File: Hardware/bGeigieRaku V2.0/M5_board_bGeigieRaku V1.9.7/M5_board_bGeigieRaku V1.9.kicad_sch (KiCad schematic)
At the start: 26 parts, among them J1 M5 2x15 pin, J10 QI GND, J11 QI charger Plus, J2 Geiger, J3 GPS, J4 Geiger 2, J7 Conn_01x14_Female, J8 QI charger GND, J9 QI Plus, Q1 IRF4905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

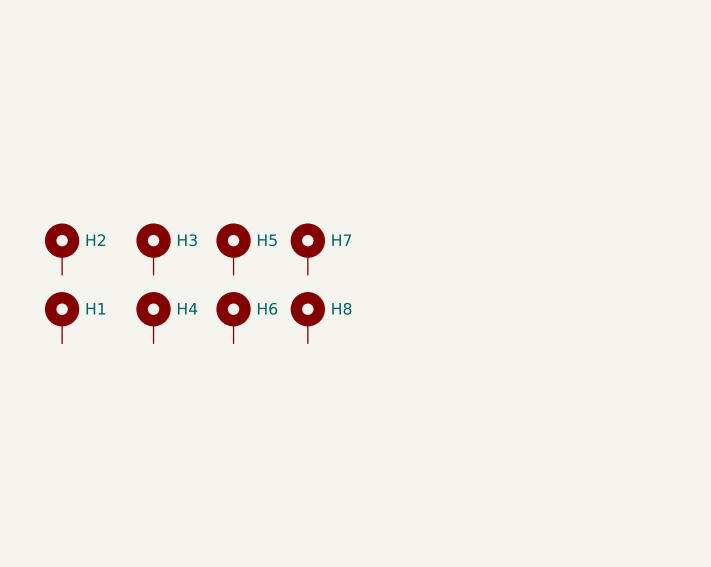
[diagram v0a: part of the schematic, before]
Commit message: alighed holes
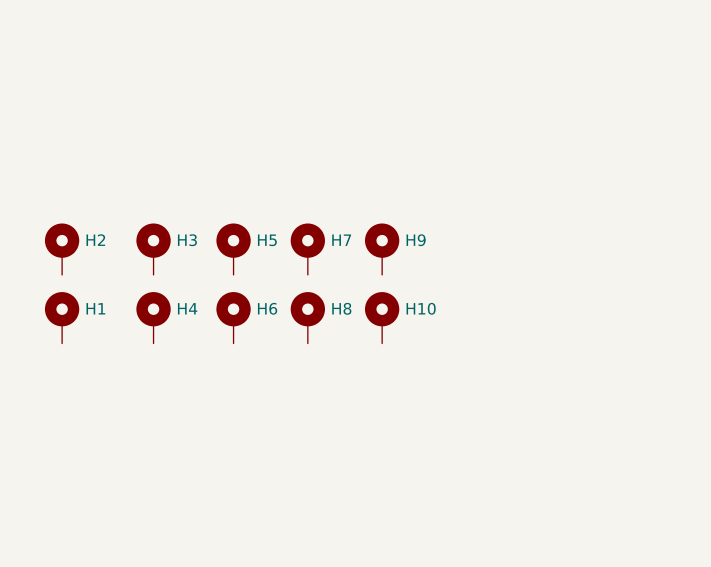
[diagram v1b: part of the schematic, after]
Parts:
- added H10, H9: MountingHole_Pad, MountingHole:MountingHole_3.2mm_M3, symbol Mechanical:MountingHole_Pad
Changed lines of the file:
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@@
+    (pin "1")
+  )
+  (symbol (lib_id "Mechanical:MountingHole_Pad") (at 241.3 116.84 0) (unit 1)
+    (in_bom yes) (on_board yes)
+    (property "Reference" "H9" (id 0) (at 243.84 115.57 0)
+      (effects (font (size 1.27 1.27)) (justify left))
+    )
+    (property "Value" "MountingHole_Pad" (id 1) (at 243.8402 117.8624 0)
+      (effects (font (size 1.27 1.27)) (justify left) hide)
+    )
+    (property "Footprint" "MountingHole:MountingHole_3.2mm_M3" (id 2) (at 241.3 116.84 0)
+      (effects (font (size 1.27 1.27)) hide)
+    )
+    (property "Datasheet" "~" (id 3) (at 241.3 116.84 0)
+      (effects (font (size 1.27 1.27)) hide)
+    )
+    (pin "1")
+  )
+  (symbol (lib_id "Mechanical:MountingHole_Pad") (at 241.3 124.46 0) (unit 1)
+    (in_bom yes) (on_board yes)
+    (property "Reference" "H10" (id 0) (at 243.84 123.19 0)
+      (effects (font (size 1.27 1.27)) (justify left))
+    )
+    (property "Value" "MountingHole_Pad" (id 1) (at 243.8398 125.4822 0)
+      (effects (font (size 1.27 1.27)) (justify left) hide)
+    )
+    (property "Footprint" "MountingHole:MountingHole_3.2mm_M3" (id 2) (at 241.3 124.46 0)
+      (effects (font (size 1.27 1.27)) hide)
+    )
+    (property "Datasheet" "~" (id 3) (at 241.3 124.46 0)
+      (effects (font (size 1.27 1.27)) hide)
+    )
     (pin "1")
   )
@@
       (reference "H8") (unit 1) (value "MountingHole_Pad") (footprint "MountingHole:MountingHole_3.2mm_M3")
     )
+    (path "/cd5e07e4-0c52-4526-99de-27f6a1504ee0"
+      (reference "H9") (unit 1) (value "MountingHole_Pad") (footprint "MountingHole:MountingHole_3.2mm_M3")
+    )
+    (path "/33accb9f-62b7-4730-ac41-d79864f006ad"
+      (reference "H10") (unit 1) (value "MountingHole_Pad") (footprint "MountingHole:MountingHole_3.2mm_M3")
+    )
     (path "/00000000-0000-0000-0000-00005d532c3e"

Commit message: Update V1.9.7 board.
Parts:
- removed D1, D2: DIODE, Diode_THT:D_DO-15_P15.24mm_Horizontal, symbol pspice:DIODE
- removed Q1, Q2: IRF4905, Package_TO_SOT_THT:TO-220-3_Vertical, symbol Transistor_FET:IRF4905
- added D1, D2: 1N4001, Diode_THT:D_DO-41_SOD81_P10.16mm_Horizontal, symbol Diode:1N4001
- added J5: Extra support header, Connector_PinHeader_2.54mm:PinHeader_1x02_P2.54mm_Vertical, symbol Connector:Conn_01x02_Male
- added Q1, Q2: IRFR9024, Package_TO_SOT_THT:TO-251-3_Vertical, symbol IRFR9024:IRFR9024
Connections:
- net GND: now also Q1.1, Q2.1
- net VBATT: now also D2.1 (K), Q2.3
- net at BT1.1 (+): now also D1.1 (K), D2.2 (A), Q1.3, Q2.2
- net at J11.1 (Pin_1), J11.2 (Pin_2): now also D1.2 (A), Q1.2
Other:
- note added: "Fix pin numbers and names on Q1 and Q2"

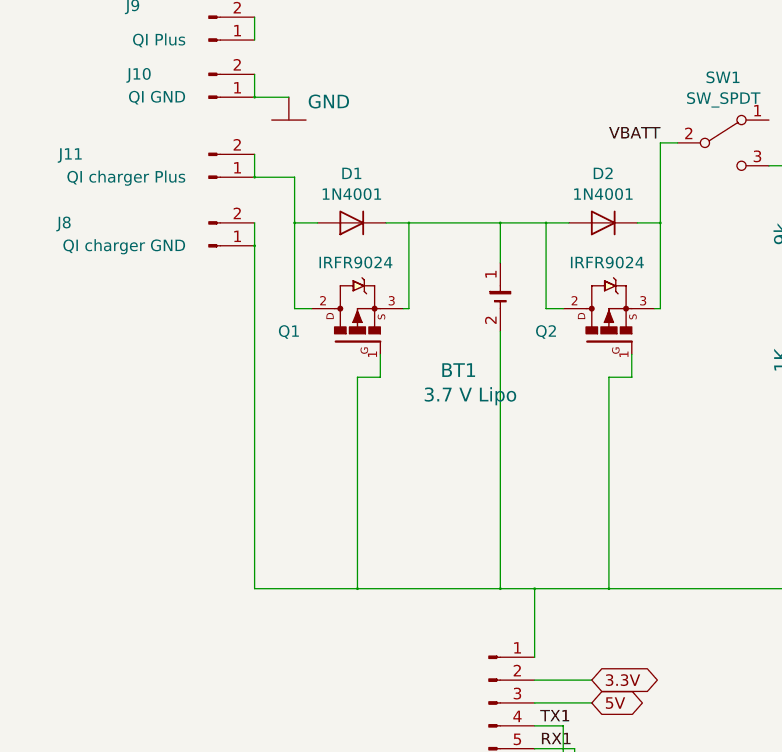
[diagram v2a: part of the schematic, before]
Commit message: Remove  Q1 and D1 (mosfet proteting TP4056)
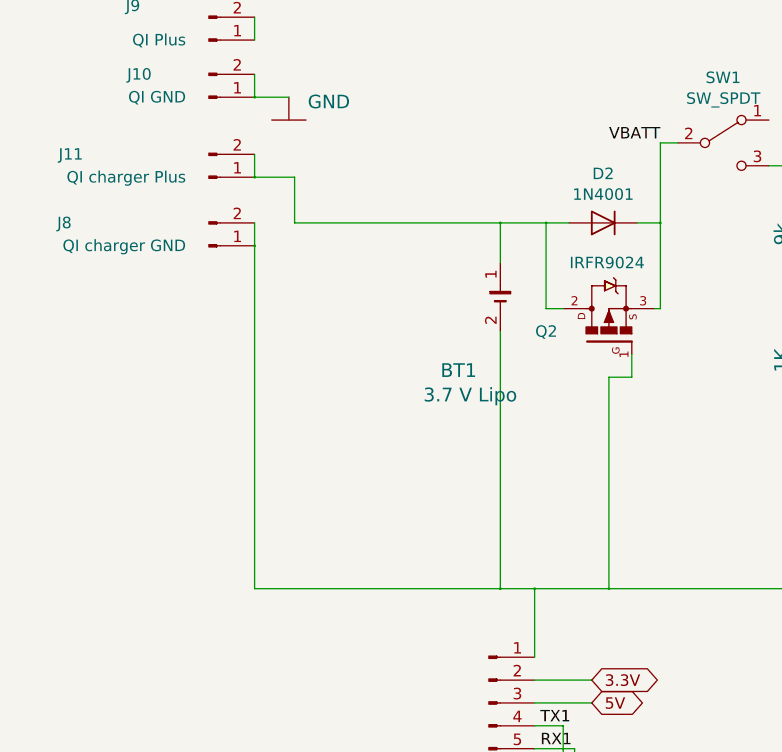
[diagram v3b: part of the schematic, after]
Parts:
- removed D1: 1N4001, Diode_THT:D_DO-41_SOD81_P10.16mm_Horizontal, symbol Diode:1N4001
- removed Q1: IRFR9024, Package_TO_SOT_THT:TO-251-3_Vertical, symbol IRFR9024:IRFR9024
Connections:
- net at BT1.1 (+), D2.2 (A), Q2.2: now also J11.1 (Pin_1), J11.2 (Pin_2)

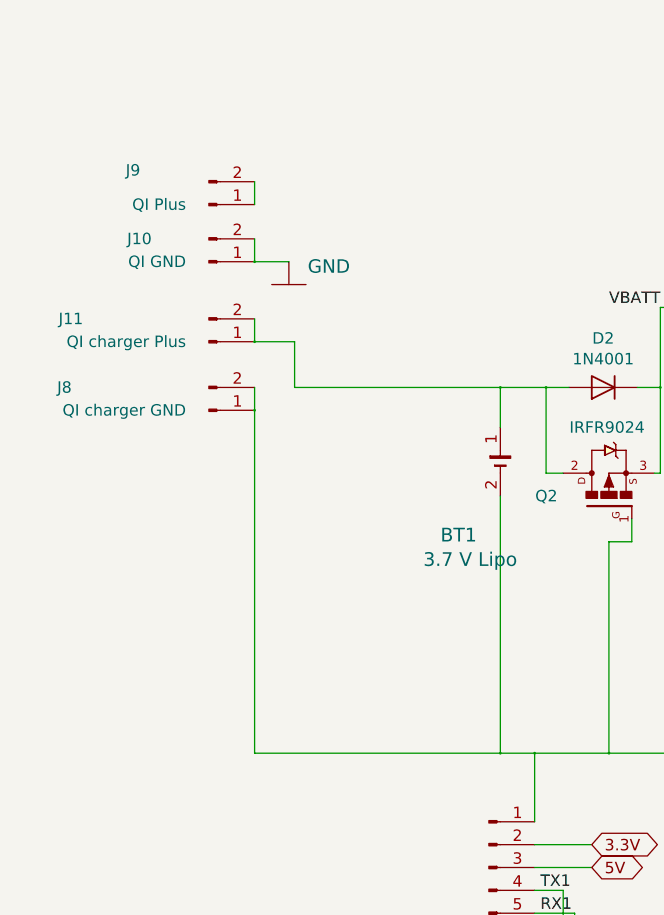
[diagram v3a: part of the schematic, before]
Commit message: Moved display 1mm to the left to get it centered.
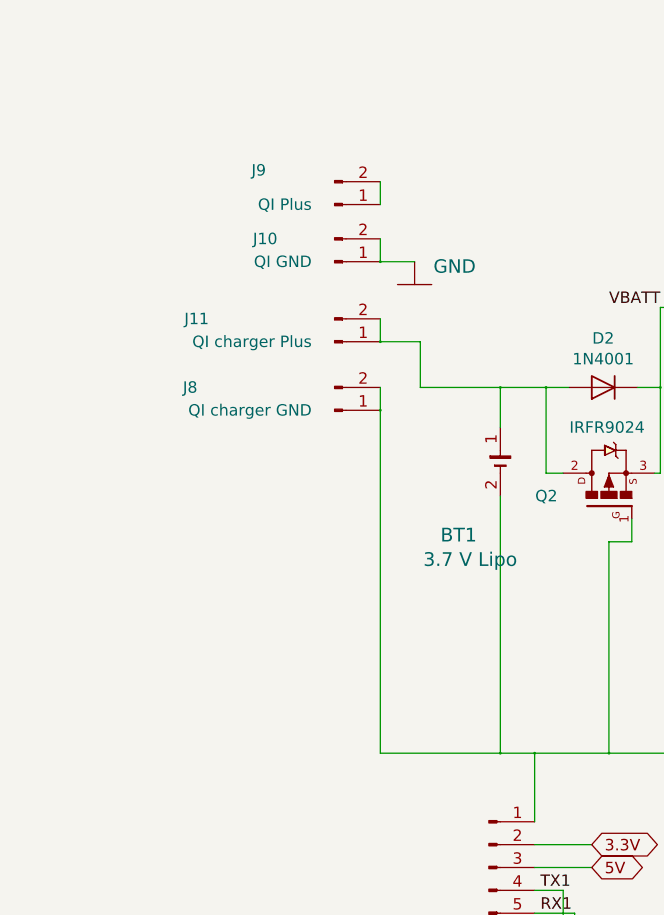
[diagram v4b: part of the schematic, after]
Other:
- moved on the sheet: J10, J11, J8, J9
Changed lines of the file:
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@@
     (date "sam. 04 avril 2015")
   )
-  (junction (at 55.88 71.12) (diameter 0.3048) (color 0 0 0 0))
-  (junction (at 55.88 80.01) (diameter 0.3048) (color 0 0 0 0))
-  (junction (at 55.88 87.63) (diameter 0.3048) (color 0 0 0 0))
+  (junction (at 69.85 71.12) (diameter 0.3048) (color 0 0 0 0))
+  (junction (at 69.85 80.01) (diameter 0.3048) (color 0 0 0 0))
+  (junction (at 69.85 87.63) (diameter 0.3048) (color 0 0 0 0))
   (junction (at 83.185 85.09) (diameter 0.3048) (color 0 0 0 0))
   (junction (at 83.185 125.73) (diameter 0.3048) (color 0 0 0 0))
@@
   (junction (at 186.69 82.55) (diameter 0.3048) (color 0 0 0 0))
   (junction (at 187.96 69.85) (diameter 0.3048) (color 0 0 0 0))
-  (wire (pts (xy 55.88 62.23) (xy 55.88 64.77))
-    (stroke (width 0) (type solid) (color 0 0 0 0))
-  )
-  (wire (pts (xy 55.88 68.58) (xy 55.88 71.12))
-    (stroke (width 0) (type solid) (color 0 0 0 0))
-  )
-  (wire (pts (xy 55.88 71.12) (xy 59.69 71.12))
-    (stroke (width 0) (type solid) (color 0 0 0 0))
-  )
-  (wire (pts (xy 55.88 77.47) (xy 55.88 80.01))
-    (stroke (width 0) (type solid) (color 0 0 0 0))
-  )
-  (wire (pts (xy 55.88 80.01) (xy 60.325 80.01))
-    (stroke (width 0) (type solid) (color 0 0 0 0))
-  )
-  (wire (pts (xy 55.88 85.09) (xy 55.88 87.63))
-    (stroke (width 0) (type solid) (color 0 0 0 0))
-  )
-  (wire (pts (xy 55.88 87.63) (xy 55.88 125.73))
-    (stroke (width 0) (type solid) (color 0 0 0 0))
-  )
-  (wire (pts (xy 55.88 125.73) (xy 83.185 125.73))
-    (stroke (width 0) (type solid) (color 0 0 0 0))
-  )
-  (wire (pts (xy 60.325 80.01) (xy 60.325 85.09))
-    (stroke (width 0) (type solid) (color 0 0 0 0))
-  )
-  (wire (pts (xy 60.325 85.09) (xy 83.185 85.09))
+  (wire (pts (xy 69.85 62.23) (xy 69.85 64.77))
+    (stroke (width 0) (type solid) (color 0 0 0 0))
+  )
+  (wire (pts (xy 69.85 68.58) (xy 69.85 71.12))
+    (stroke (width 0) (type solid) (color 0 0 0 0))
+  )
+  (wire (pts (xy 69.85 71.12) (xy 73.66 71.12))
+    (stroke (width 0) (type solid) (color 0 0 0 0))
+  )
+  (wire (pts (xy 69.85 77.47) (xy 69.85 80.01))
+    (stroke (width 0) (type solid) (color 0 0 0 0))
+  )
+  (wire (pts (xy 69.85 80.01) (xy 74.295 80.01))
+    (stroke (width 0) (type solid) (color 0 0 0 0))
+  )
+  (wire (pts (xy 69.85 85.09) (xy 69.85 87.63))
+    (stroke (width 0) (type solid) (color 0 0 0 0))
+  )
+  (wire (pts (xy 69.85 87.63) (xy 69.85 125.73))
+    (stroke (width 0) (type solid) (color 0 0 0 0))
+  )
+  (wire (pts (xy 69.85 125.73) (xy 83.185 125.73))
+    (stroke (width 0) (type solid) (color 0 0 0 0))
+  )
+  (wire (pts (xy 74.295 80.01) (xy 74.295 85.09))
+    (stroke (width 0) (type solid) (color 0 0 0 0))
+  )
+  (wire (pts (xy 74.295 85.09) (xy 83.185 85.09))
     (stroke (width 0) (type solid) (color 0 0 0 0))
   )
@@
     )
   )
-  (symbol (lib_id "bGeigieRaku-V2-rescue:GND-bGeigieNano_V1.1.5") (at 59.69 73.66 0) (unit 1)
+  (symbol (lib_id "bGeigieRaku-V2-rescue:GND-bGeigieNano_V1.1.5") (at 73.66 73.66 0) (unit 1)
     (in_bom yes) (on_board yes)
-    (property "Reference" "#GND0101" (id 0) (at 59.69 73.66 0)
-      (effects (font (size 1.27 1.27)) hide)
-    )
-    (property "Value" "GND" (id 1) (at 64.135 71.6534 0)
+    (property "Reference" "#GND0101" (id 0) (at 73.66 73.66 0)
+      (effects (font (size 1.27 1.27)) hide)
+    )
+    (property "Value" "GND" (id 1) (at 78.105 71.6534 0)
       (effects (font (size 1.4986 1.4986)))
     )
-    (property "Footprint" "" (id 2) (at 59.69 73.66 0)
-      (effects (font (size 1.27 1.27)) hide)
-    )
-    (property "Datasheet" "" (id 3) (at 59.69 73.66 0)
+    (property "Footprint" "" (id 2) (at 73.66 73.66 0)
+      (effects (font (size 1.27 1.27)) hide)
+    )
+    (property "Datasheet" "" (id 3) (at 73.66 73.66 0)
       (effects (font (size 1.27 1.27)) hide)
     )
@@
     (pin "1")
   )
-  (symbol (lib_id "Connector:Conn_01x02_Male") (at 50.8 64.77 0) (mirror x) (unit 1)
+  (symbol (lib_id "Connector:Conn_01x02_Male") (at 64.77 64.77 0) (mirror x) (unit 1)
     (in_bom yes) (on_board yes)
-    (property "Reference" "J9" (id 0) (at 43.18 60.96 0)
-      (effects (font (size 1.27 1.27)) (justify right))
-    )
-    (property "Value" "QI Plus" (id 1) (at 48.26 64.77 0)
-      (effects (font (size 1.27 1.27)) (justify right))
-    )
-    (property "Footprint" "Connector_PinHeader_2.54mm:PinHeader_1x02_P2.54mm_Vertical" (id 2) (at 50.8 64.77 0)
-      (effects (font (size 1.27 1.27)) hide)
-    )
-    (property "Datasheet" "~" (id 3) (at 50.8 64.77 0)
+    (property "Reference" "J9" (id 0) (at 57.15 60.96 0)
+      (effects (font (size 1.27 1.27)) (justify right))
+    )
+    (property "Value" "QI Plus" (id 1) (at 62.23 64.77 0)
+      (effects (font (size 1.27 1.27)) (justify right))
+    )
+    (property "Footprint" "Connector_PinHeader_2.54mm:PinHeader_1x02_P2.54mm_Vertical" (id 2) (at 64.77 64.77 0)
+      (effects (font (size 1.27 1.27)) hide)
+    )
+    (property "Datasheet" "~" (id 3) (at 64.77 64.77 0)
       (effects (font (size 1.27 1.27)) hide)
     )
@@
     (pin "2")
   )
-  (symbol (lib_id "Connector:Conn_01x02_Male") (at 50.8 71.12 0) (mirror x) (unit 1)
+  (symbol (lib_id "Connector:Conn_01x02_Male") (at 64.77 71.12 0) (mirror x) (unit 1)
     (in_bom yes) (on_board yes)
-    (property "Reference" "J10" (id 0) (at 44.45 68.58 0)
-      (effects (font (size 1.27 1.27)) (justify right))
-    )
-    (property "Value" "QI GND" (id 1) (at 48.26 71.12 0)
-      (effects (font (size 1.27 1.27)) (justify right))
-    )
-    (property "Footprint" "Connector_PinHeader_2.54mm:PinHeader_1x02_P2.54mm_Vertical" (id 2) (at 50.8 71.12 0)
-      (effects (font (size 1.27 1.27)) hide)
-    )
-    (property "Datasheet" "~" (id 3) (at 50.8 71.12 0)
+    (property "Reference" "J10" (id 0) (at 58.42 68.58 0)
+      (effects (font (size 1.27 1.27)) (justify right))
+    )
+    (property "Value" "QI GND" (id 1) (at 62.23 71.12 0)
+      (effects (font (size 1.27 1.27)) (justify right))
+    )
+    (property "Footprint" "Connector_PinHeader_2.54mm:PinHeader_1x02_P2.54mm_Vertical" (id 2) (at 64.77 71.12 0)
+      (effects (font (size 1.27 1.27)) hide)
+    )
+    (property "Datasheet" "~" (id 3) (at 64.77 71.12 0)
       (effects (font (size 1.27 1.27)) hide)
     )
@@
     (pin "2")
   )
-  (symbol (lib_id "Connector:Conn_01x02_Male") (at 50.8 80.01 0) (mirror x) (unit 1)
+  (symbol (lib_id "Connector:Conn_01x02_Male") (at 64.77 80.01 0) (mirror x) (unit 1)
     (in_bom yes) (on_board yes)
-    (property "Reference" "J11" (id 0) (at 36.83 77.47 0)
-      (effects (font (size 1.27 1.27)) (justify right))
-    )
-    (property "Value" "QI charger Plus" (id 1) (at 48.26 80.01 0)
-      (effects (font (size 1.27 1.27)) (justify right))
-    )
-    (property "Footprint" "Connector_PinHeader_2.54mm:PinHeader_1x02_P2.54mm_Vertical" (id 2) (at 50.8 80.01 0)
-      (effects (font (size 1.27 1.27)) hide)
-    )
-    (property "Datasheet" "~" (id 3) (at 50.8 80.01 0)
+    (property "Reference" "J11" (id 0) (at 50.8 77.47 0)
+      (effects (font (size 1.27 1.27)) (justify right))
+    )
+    (property "Value" "QI charger Plus" (id 1) (at 62.23 80.01 0)
+      (effects (font (size 1.27 1.27)) (justify right))
+    )
+    (property "Footprint" "Connector_PinHeader_2.54mm:PinHeader_1x02_P2.54mm_Vertical" (id 2) (at 64.77 80.01 0)
+      (effects (font (size 1.27 1.27)) hide)
+    )
+    (property "Datasheet" "~" (id 3) (at 64.77 80.01 0)
       (effects (font (size 1.27 1.27)) hide)
     )
@@
     (pin "2")
   )
-  (symbol (lib_id "Connector:Conn_01x02_Male") (at 50.8 87.63 0) (mirror x) (unit 1)
+  (symbol (lib_id "Connector:Conn_01x02_Male") (at 64.77 87.63 0) (mirror x) (unit 1)
     (in_bom yes) (on_board yes)
-    (property "Reference" "J8" (id 0) (at 35.56 85.09 0)
-      (effects (font (size 1.27 1.27)) (justify right))
-    )
-    (property "Value" "QI charger GND" (id 1) (at 48.26 87.63 0)
-      (effects (font (size 1.27 1.27)) (justify right))
-    )
-    (property "Footprint" "Connector_PinHeader_2.54mm:PinHeader_1x02_P2.54mm_Vertical" (id 2) (at 50.8 87.63 0)
-      (effects (font (size 1.27 1.27)) hide)
-    )
-    (property "Datasheet" "~" (id 3) (at 50.8 87.63 0)
-      (effects (font (size 1.27 1.27)) hide)
-    )
+    (property "Reference" "J8" (id 0) (at 49.53 85.09 0)
+      (effects (font (size 1.27 1.27)) (justify right))
+    )
+    (property "Value" "QI charger GND" (id 1) (at 62.23 87.63 0)
+      (effects (font (size 1.27 1.27)) (justify right))
+    )
+    (property "Footprint" "Connector_PinHeader_2.54mm:PinHeader_1x02_P2.54mm_Vertical" (id 2) (at 64.77 87.63 0)
+      (effects (font (size 1.27 1.27)) hide)
+    )
+    (property "Datasheet" "~" (id 3) (at 64.77 87.63 0)
+      (effects (font (size 1.27 1.27)) hide)
+    )

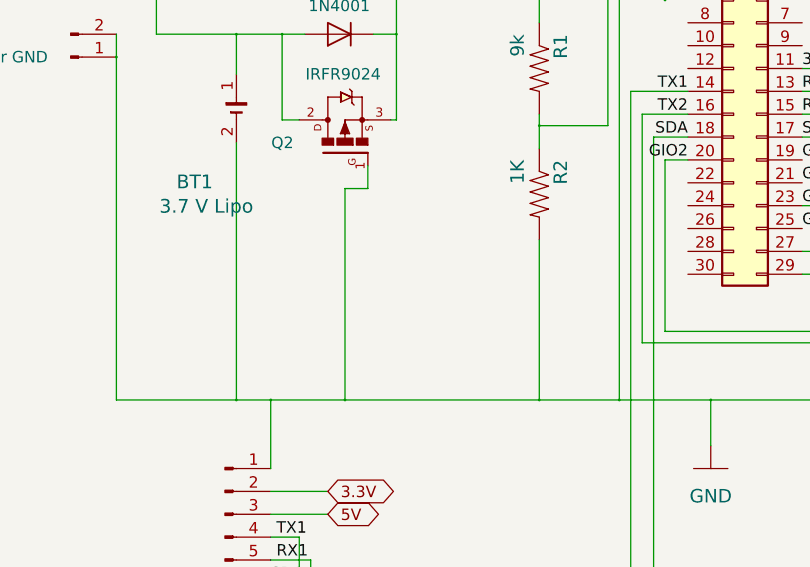
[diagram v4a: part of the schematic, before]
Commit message: V1.9.8 hardware and LiPo and charger changes
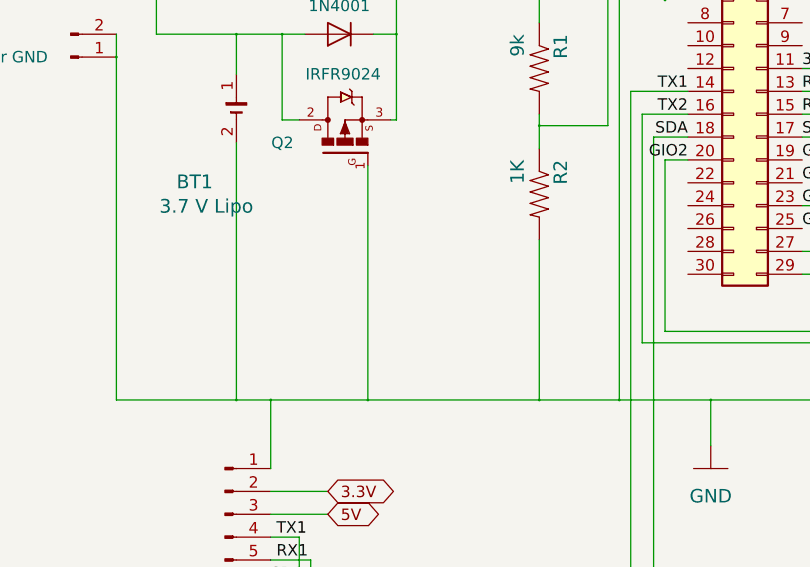
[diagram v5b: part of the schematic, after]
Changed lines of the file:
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@@
   (junction (at 86.995 125.73) (diameter 0.3048) (color 0 0 0 0))
   (junction (at 88.265 85.09) (diameter 0.3048) (color 0 0 0 0))
-  (junction (at 95.25 125.73) (diameter 0.3048) (color 0 0 0 0))
+  (junction (at 97.79 125.73) (diameter 0.3048) (color 0 0 0 0))
   (junction (at 100.965 85.09) (diameter 0.3048) (color 0 0 0 0))
   (junction (at 116.84 78.74) (diameter 0.3048) (color 0 0 0 0))
@@
     (stroke (width 0) (type solid) (color 0 0 0 0))
   )
+  (wire (pts (xy 86.995 125.73) (xy 97.79 125.73))
+    (stroke (width 0) (type solid) (color 0 0 0 0))
+  )
   (wire (pts (xy 86.995 133.35) (xy 86.995 125.73))
     (stroke (width 0) (type solid) (color 0 0 0 0))
@@
     (stroke (width 0) (type solid) (color 0 0 0 0))
   )
-  (wire (pts (xy 95.25 102.235) (xy 95.25 125.73))
-    (stroke (width 0) (type solid) (color 0 0 0 0))
-  )
-  (wire (pts (xy 95.25 102.235) (xy 97.79 102.235))
-    (stroke (width 0) (type solid) (color 0 0 0 0))
-  )
-  (wire (pts (xy 95.25 125.73) (xy 86.995 125.73))
-    (stroke (width 0) (type solid) (color 0 0 0 0))
-  )
-  (wire (pts (xy 95.25 125.73) (xy 116.84 125.73))
-    (stroke (width 0) (type solid) (color 0 0 0 0))
-  )
   (wire (pts (xy 95.25 151.13) (xy 86.995 151.13))
     (stroke (width 0) (type solid) (color 0 0 0 0))
@@
     (stroke (width 0) (type solid) (color 0 0 0 0))
   )
-  (wire (pts (xy 97.79 102.235) (xy 97.79 99.695))
+  (wire (pts (xy 97.79 99.695) (xy 97.79 125.73))
     (stroke (width 0) (type solid) (color 0 0 0 0))
   )
+  (wire (pts (xy 97.79 125.73) (xy 116.84 125.73))
+    (stroke (width 0) (type solid) (color 0 0 0 0))
+  )
